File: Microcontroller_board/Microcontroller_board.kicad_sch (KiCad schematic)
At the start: 0 parts

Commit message: Added two more leds and make the schematic a little bit prettier
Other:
- removed sheet PowerSupply
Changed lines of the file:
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@@
-    )
-  )
-  (sheet (at 184.15 209.55) (size 35.56 21.59) (fields_autoplaced)
-    (stroke (width 0.1524) (type solid))
-    (fill (color 0 0 0 0.0000))
-    (property "Sheetname" "PowerSupply" (at 184.15 208.8384 0)
-      (effects (font (size 1.27 1.27)) (justify left bottom))
-    )
-    (property "Sheetfile" "PowerSupply.kicad_sch" (at 184.15 231.7246 0)
-      (effects (font (size 1.27 1.27)) (justify left top))
-    )
-    (instances
-      (project "Microcontroller_board"
-        (path "/8159cf7c-7477-4d57-9227-35cab5afcf8d" (page "8"))
-      )
     )
   )

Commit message: Added led interface
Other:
- sheet Led interface ports: added LED_CONTROL; removed none
- sheet STM32_Microcontroller ports: added LED_CONTROL; removed none
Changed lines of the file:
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@@
 (kicad_sch (version 20230121) (generator eeschema)
   (paper "A3")
+  (wire (pts (xy 242.57 142.24) (xy 242.57 161.29))
+    (stroke (width 0) (type default))
+  )
+  (wire (pts (xy 252.73 134.62) (xy 252.73 125.73))
+    (stroke (width 0) (type default))
+  )
+  (wire (pts (xy 151.13 46.99) (xy 179.07 46.99))
+    (stroke (width 0) (type default))
+  )
   (wire (pts (xy 151.13 49.53) (xy 179.07 49.53))
     (stroke (width 0) (type default))
   )
-  (wire (pts (xy 242.57 142.24) (xy 242.57 161.29))
-    (stroke (width 0) (type default))
-  )
   (wire (pts (xy 135.89 109.22) (xy 179.07 109.22))
     (stroke (width 0) (type default))
@@
     (stroke (width 0) (type default))
   )
+  (wire (pts (xy 262.89 134.62) (xy 252.73 134.62))
+    (stroke (width 0) (type default))
+  )
+  (wire (pts (xy 135.89 111.76) (xy 179.07 111.76))
+    (stroke (width 0) (type default))
+  )
+  (wire (pts (xy 252.73 125.73) (xy 226.06 125.73))
+    (stroke (width 0) (type default))
+  )
+  (wire (pts (xy 151.13 41.91) (xy 179.07 41.91))
+    (stroke (width 0) (type default))
+  )
+  (wire (pts (xy 245.11 158.75) (xy 245.11 139.7))
+    (stroke (width 0) (type default))
+  )
+  (wire (pts (xy 247.65 156.21) (xy 247.65 137.16))
+    (stroke (width 0) (type default))
+  )
+  (wire (pts (xy 226.06 114.3) (xy 262.89 114.3))
+    (stroke (width 0) (type default))
+  )
+  (wire (pts (xy 247.65 156.21) (xy 262.89 156.21))
+    (stroke (width 0) (type default))
+  )
+  (wire (pts (xy 245.11 139.7) (xy 226.06 139.7))
+    (stroke (width 0) (type default))
+  )
   (wire (pts (xy 151.13 44.45) (xy 179.07 44.45))
     (stroke (width 0) (type default))
   )
-  (wire (pts (xy 135.89 111.76) (xy 179.07 111.76))
-    (stroke (width 0) (type default))
-  )
-  (wire (pts (xy 245.11 158.75) (xy 245.11 139.7))
-    (stroke (width 0) (type default))
-  )
-  (wire (pts (xy 151.13 46.99) (xy 179.07 46.99))
-    (stroke (width 0) (type default))
-  )
-  (wire (pts (xy 247.65 156.21) (xy 247.65 137.16))
-    (stroke (width 0) (type default))
-  )
-  (wire (pts (xy 226.06 114.3) (xy 262.89 114.3))
-    (stroke (width 0) (type default))
-  )
-  (wire (pts (xy 247.65 156.21) (xy 262.89 156.21))
-    (stroke (width 0) (type default))
-  )
-  (wire (pts (xy 151.13 41.91) (xy 179.07 41.91))
-    (stroke (width 0) (type default))
-  )
-  (wire (pts (xy 245.11 139.7) (xy 226.06 139.7))
-    (stroke (width 0) (type default))
-  )
   (wire (pts (xy 247.65 137.16) (xy 226.06 137.16))
     (stroke (width 0) (type default))
@@
       (effects (font (size 1.27 1.27)) (justify right))
     )
+    (pin "LED_CONTROL" input (at 226.06 125.73 0)
+      (effects (font (size 1.27 1.27)) (justify right))
+    )
     (instances
       (project "Microcontroller_board"
@@
       (effects (font (size 1.27 1.27)) (justify left top))
     )
+    (pin "LED_CONTROL" input (at 262.89 134.62 180)
+      (effects (font (size 1.27 1.27)) (justify left))
+    )
     (instances
       (project "Microcontroller_board"
@@
     )
   )
-  (sheet (at 179.07 38.1) (size 45.72 49.53) (fields_autoplaced)
-    (stroke (width 0.1524) (type solid))
-    (fill (color 0 0 0 0.0000))
-    (property "Sheetname" "ESP32_Microcontroller" (at 179.07 37.3884 0)
-      (effects (font (size 1.27 1.27)) (justify left bottom))
-    )
-    (property "Sheetfile" "ESP32_Microcontroller.kicad_sch" (at 179.07 88.2146 0)
-      (effects (font (size 1.27 1.27)) (justify left top))
-    )
+  (sheet (at 179.07 30.48) (size 45.72 49.53) (fields_autoplaced)
+    (stroke (width 0.1524) (type solid))
+    (fill (color 0 0 0 0.0000))
+    (property "Sheetname" "ESP32_Microcontroller" (at 179.07 29.7684 0)
+      (effects (font (size 1.27 1.27)) (justify left bottom))
+    )
+    (property "Sheetfile" "ESP32_Microcontroller.kicad_sch" (at 179.07 80.5946 0)
+      (effects (font (size 1.27 1.27)) (justify left top))
+    )

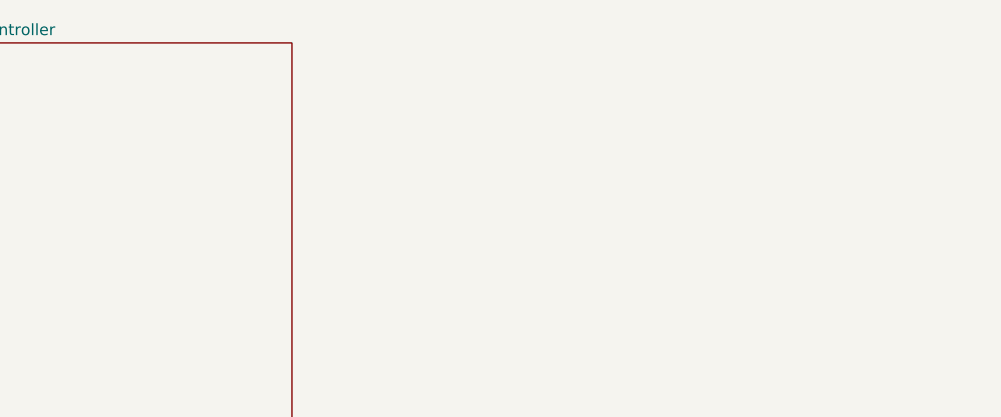
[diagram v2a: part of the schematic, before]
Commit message: Added the connector for LCD Nextion and connected to esp32
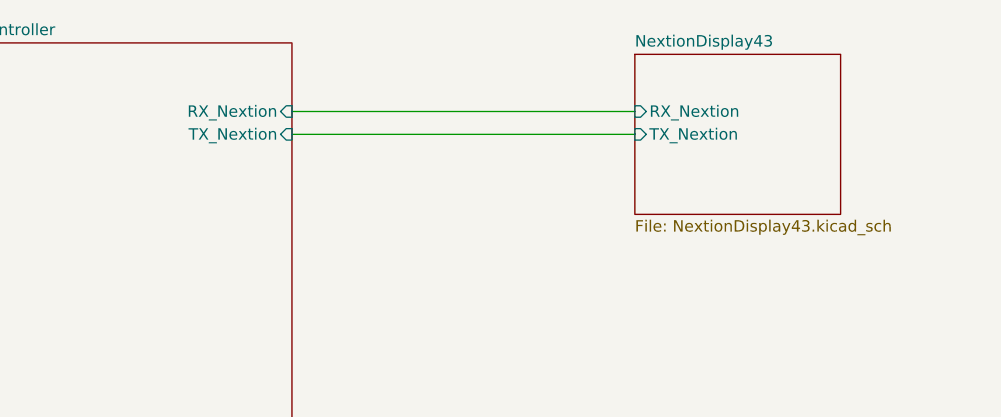
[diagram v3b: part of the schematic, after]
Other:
- added sheet NextionDisplay43 (NextionDisplay43.kicad_sch)
- sheet ESP32_Microcontroller ports: added RX_Nextion, TX_Nextion; removed none
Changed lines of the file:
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@@
+    (stroke (width 0) (type default))
+  )
+  (wire (pts (xy 224.79 40.64) (xy 262.89 40.64))
     (stroke (width 0) (type default))
   )
@@
     (stroke (width 0) (type default))
   )
+  (wire (pts (xy 224.79 38.1) (xy 262.89 38.1))
+    (stroke (width 0) (type default))
+  )
   (wire (pts (xy 262.89 158.75) (xy 245.11 158.75))
     (stroke (width 0) (type default))
@@
     )
   )
+  (sheet (at 262.89 31.75) (size 22.86 17.78) (fields_autoplaced)
+    (stroke (width 0.1524) (type solid))
+    (fill (color 0 0 0 0.0000))
+    (property "Sheetname" "NextionDisplay43" (at 262.89 31.0384 0)
+      (effects (font (size 1.27 1.27)) (justify left bottom))
+    )
+    (property "Sheetfile" "NextionDisplay43.kicad_sch" (at 262.89 50.1146 0)
+      (effects (font (size 1.27 1.27)) (justify left top))
+    )
+    (pin "RX_Nextion" input (at 262.89 38.1 180)
+      (effects (font (size 1.27 1.27)) (justify left))
+    )
+    (pin "TX_Nextion" input (at 262.89 40.64 180)
+      (effects (font (size 1.27 1.27)) (justify left))
+    )
+    (instances
+      (project "Microcontroller_board"
+        (path "/8159cf7c-7477-4d57-9227-35cab5afcf8d" (page "10"))
+      )
+    )
+  )
   (sheet (at 179.07 30.48) (size 45.72 49.53) (fields_autoplaced)
     (stroke (width 0.1524) (type solid))
@@
       (effects (font (size 1.27 1.27)) (justify left))
     )
-    (instances
+    (pin "RX_Nextion" input (at 224.79 38.1 0)
+      (effects (font (size 1.27 1.27)) (justify right))
+    )
+    (pin "TX_Nextion" input (at 224.79 40.64 0)
+      (effects (font (size 1.27 1.27)) (justify right))
+    )
+    (instances

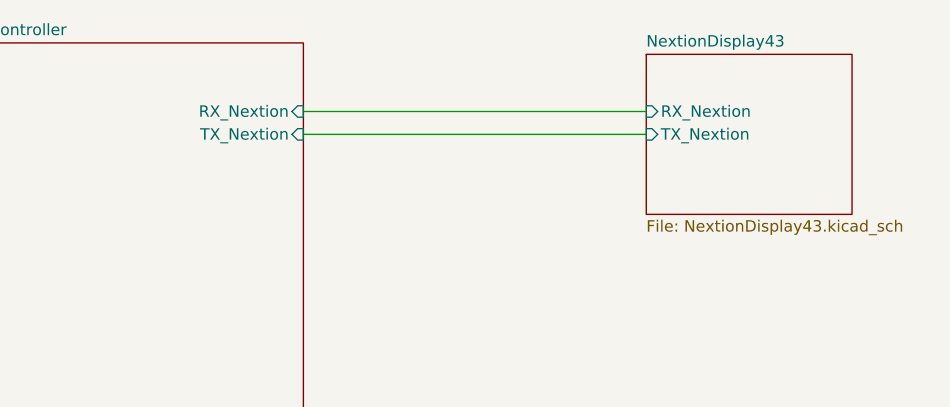
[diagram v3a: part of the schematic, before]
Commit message: Correct the labels for nextion
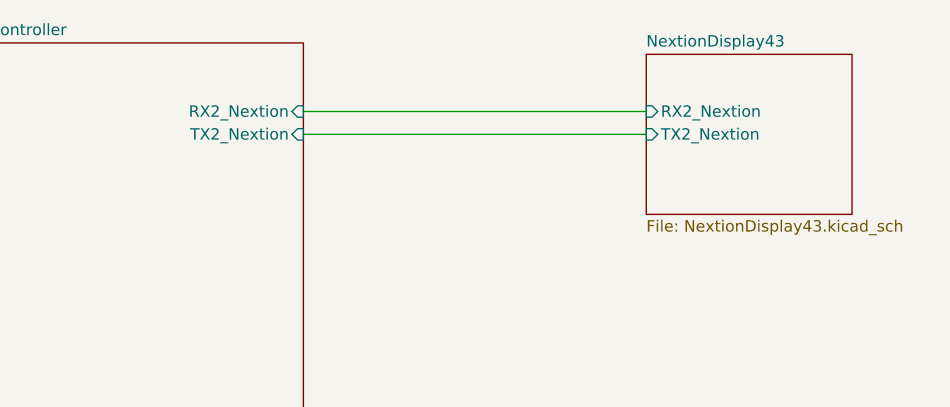
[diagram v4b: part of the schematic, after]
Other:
- sheet ESP32_Microcontroller ports: added RX2_Nextion, TX2_Nextion; removed RX_Nextion, TX_Nextion
- sheet NextionDisplay43 ports: added RX2_Nextion, TX2_Nextion; removed RX_Nextion, TX_Nextion
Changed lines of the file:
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@@
       (effects (font (size 1.27 1.27)) (justify left top))
     )
-    (pin "RX_Nextion" input (at 262.89 38.1 180)
+    (pin "RX2_Nextion" input (at 262.89 38.1 180)
       (effects (font (size 1.27 1.27)) (justify left))
     )
-    (pin "TX_Nextion" input (at 262.89 40.64 180)
+    (pin "TX2_Nextion" input (at 262.89 40.64 180)
       (effects (font (size 1.27 1.27)) (justify left))
     )
@@
       (effects (font (size 1.27 1.27)) (justify left))
     )
-    (pin "RX_Nextion" input (at 224.79 38.1 0)
+    (pin "RX2_Nextion" input (at 224.79 38.1 0)
       (effects (font (size 1.27 1.27)) (justify right))
     )
-    (pin "TX_Nextion" input (at 224.79 40.64 0)
+    (pin "TX2_Nextion" input (at 224.79 40.64 0)
       (effects (font (size 1.27 1.27)) (justify right))
     )

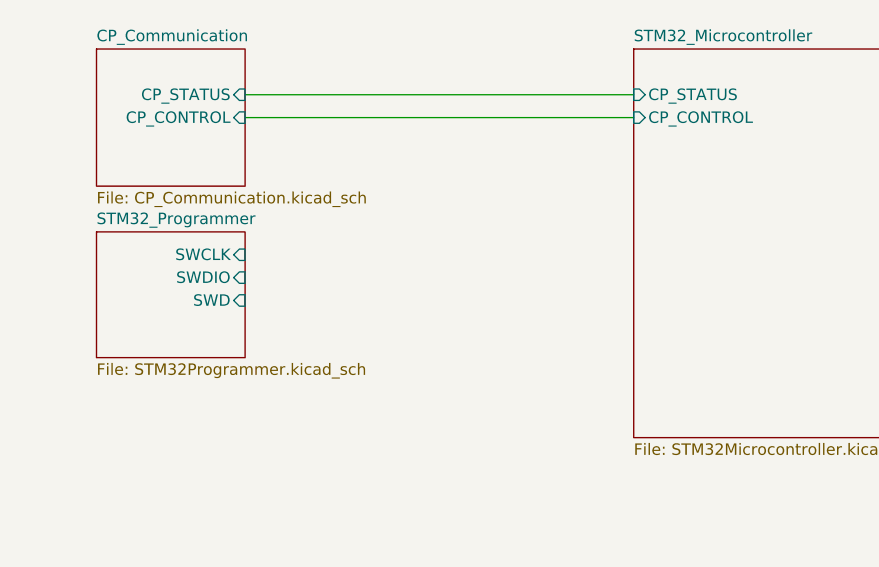
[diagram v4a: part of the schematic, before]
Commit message: Added connector for st link programmer
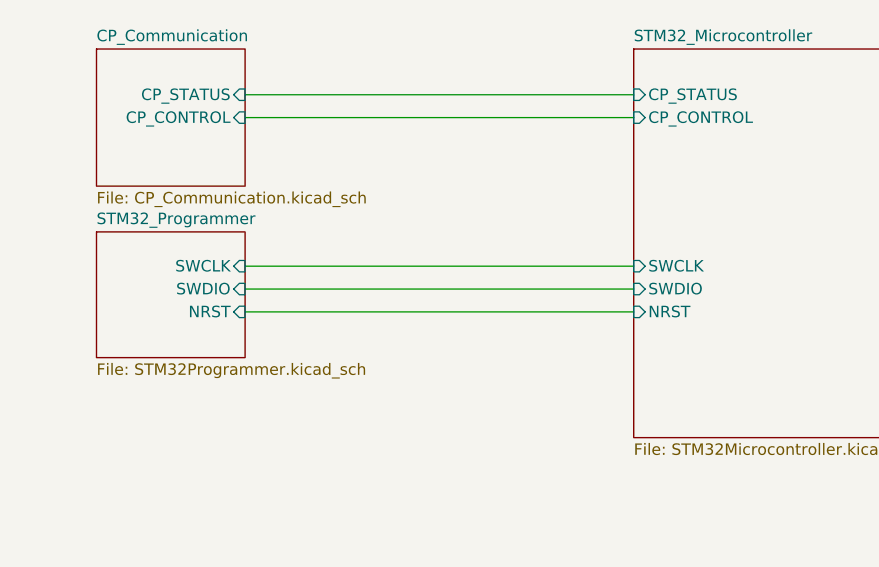
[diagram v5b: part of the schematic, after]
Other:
- sheet STM32_Microcontroller ports: added NRST, SWCLK, SWDIO; removed none
- sheet STM32_Programmer ports: added NRST; removed SWD
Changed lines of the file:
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@@
+    (stroke (width 0) (type default))
+  )
+  (wire (pts (xy 135.89 133.35) (xy 179.07 133.35))
     (stroke (width 0) (type default))
   )
@@
     (stroke (width 0) (type default))
   )
+  (wire (pts (xy 135.89 128.27) (xy 179.07 128.27))
+    (stroke (width 0) (type default))
+  )
   (wire (pts (xy 247.65 156.21) (xy 247.65 137.16))
     (stroke (width 0) (type default))
@@
   )
   (wire (pts (xy 151.13 44.45) (xy 179.07 44.45))
+    (stroke (width 0) (type default))
+  )
+  (wire (pts (xy 135.89 130.81) (xy 179.07 130.81))
     (stroke (width 0) (type default))
   )
@@
     (pin "LED_CONTROL" input (at 226.06 125.73 0)
       (effects (font (size 1.27 1.27)) (justify right))
+    )
+    (pin "NRST" input (at 179.07 133.35 180)
+      (effects (font (size 1.27 1.27)) (justify left))
+    )
+    (pin "SWCLK" input (at 179.07 128.27 180)
+      (effects (font (size 1.27 1.27)) (justify left))
+    )
+    (pin "SWDIO" input (at 179.07 130.81 180)
+      (effects (font (size 1.27 1.27)) (justify left))
     )
     (instances
@@
       (effects (font (size 1.27 1.27)) (justify left top))
     )
-    (pin "SWCLK" input (at 135.89 127 0)
+    (pin "SWCLK" input (at 135.89 128.27 0)
       (effects (font (size 1.27 1.27)) (justify right))
     )
-    (pin "SWDIO" input (at 135.89 129.54 0)
+    (pin "SWDIO" input (at 135.89 130.81 0)
       (effects (font (size 1.27 1.27)) (justify right))
     )
-    (pin "SWD" input (at 135.89 132.08 0)
+    (pin "NRST" input (at 135.89 133.35 0)
       (effects (font (size 1.27 1.27)) (justify right))
     )
